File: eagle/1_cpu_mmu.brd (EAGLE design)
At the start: 160 x 100 mm, 49 parts, among them IC1 MT5C6408, IC10 74LS157N, IC11 74LS157N, IC12 74LS00N, IC13 74LS157N, IC14 74LS157N, IC16 74LS08N, IC17 74LS32N, IC19 74LS32N, IC2 MT5C6408, IC20 74LS02N, IC21 74LS374N, IC3 74LS27N, IC4 74LS20N, IC5 74LS08N, IC6 74LS245N, IC7 74LS245N, IC8 74LS32N, IC9 74LS157N

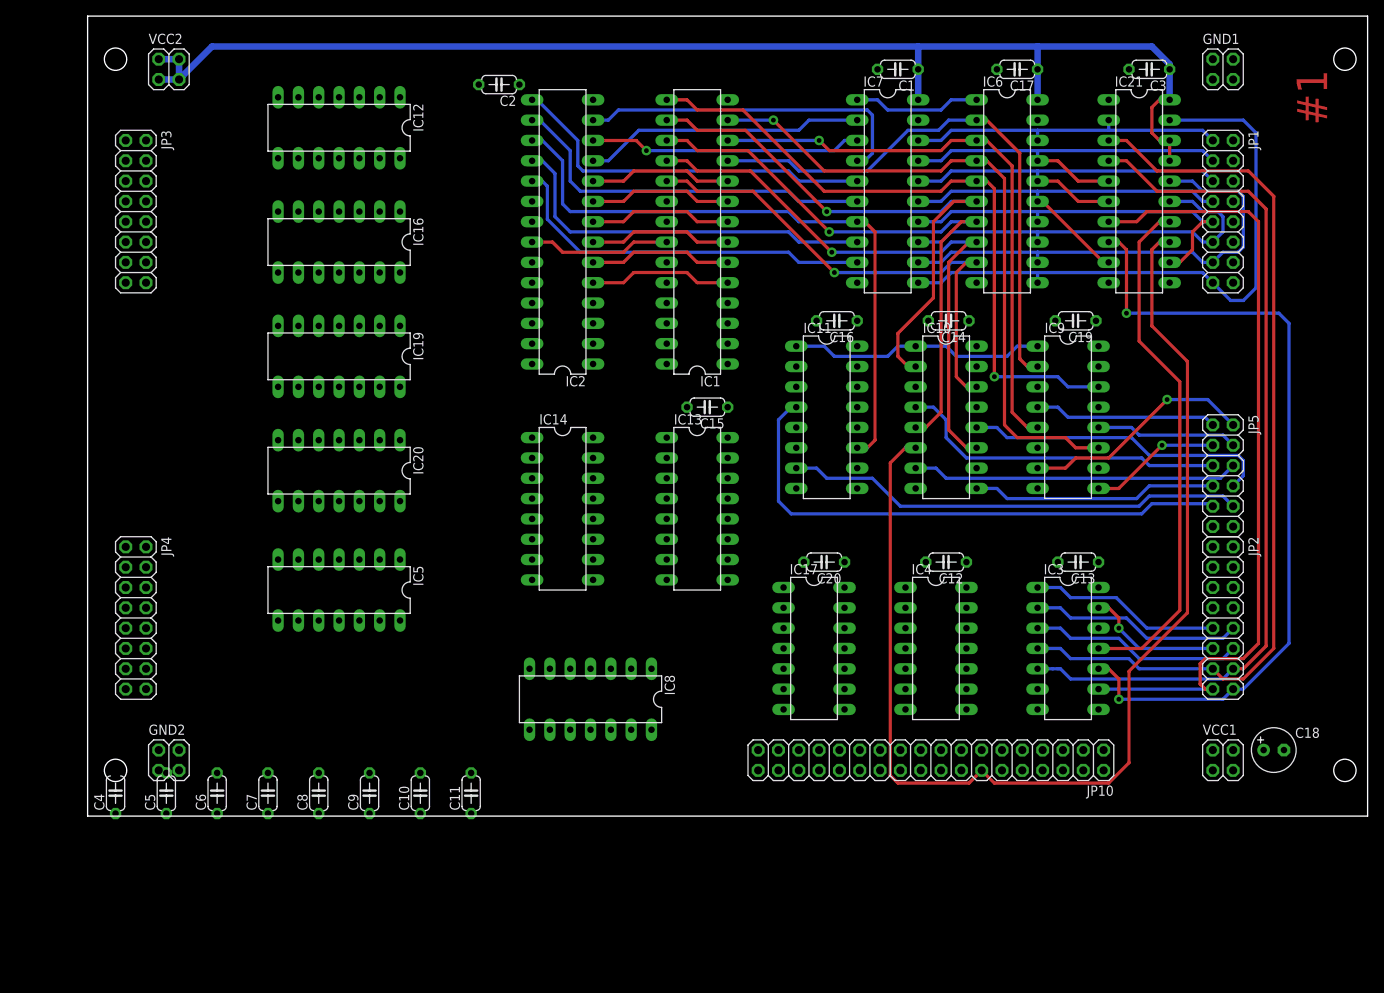
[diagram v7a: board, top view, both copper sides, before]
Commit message: MMU and Memory board updates, removed mem_ext board (obsolete)
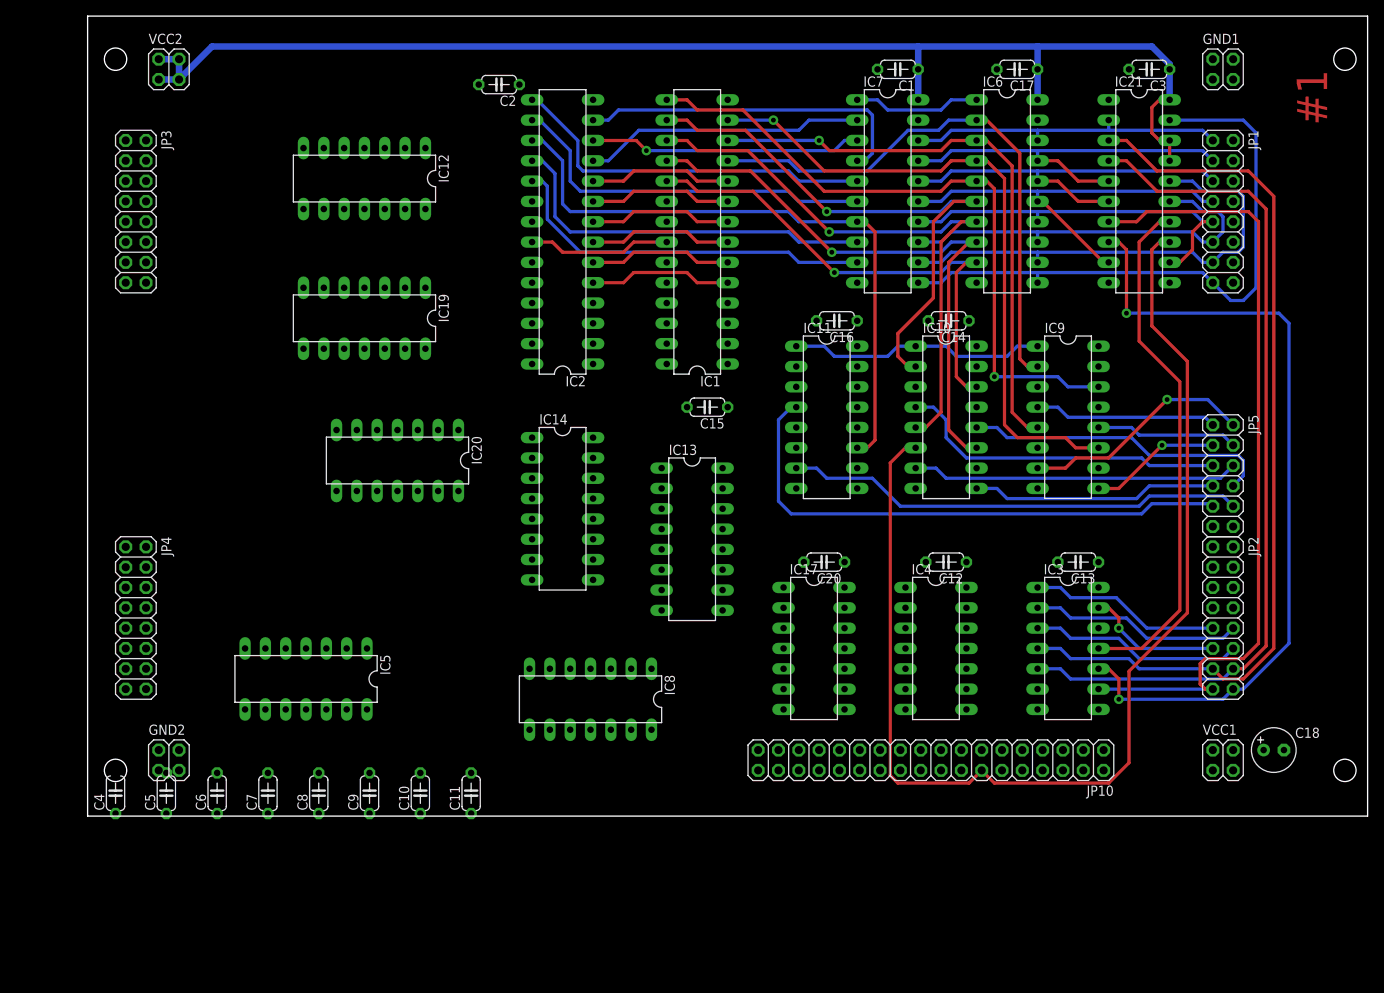
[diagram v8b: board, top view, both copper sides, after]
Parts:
- removed C19: 100n, rcl:C050-024X044
- removed IC16: 74LS08N, 74xx-eu:DIL14
- moved IC5 11.9 mm to (27.3, 17.1)
- moved IC20 7.41 mm to (38.7, 44.5)
- moved IC12 7.10 mm to (34.6, 79.7)
- moved IC19 5.72 mm to (34.6, 62.2)
- moved IC13 3.86 mm to (75.6, 34.6)
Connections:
- net +5V: no longer C19.1, IC16.14
- net /FS: no longer IC20.6
- net /NP_FAULT: no longer IC16.4
- net /WR_FAULT: no longer IC16.5
- net ABUS7: now also IC20.6
- net FAULT: now also IC20.8, IC20.9
- net GND: no longer C19.2, IC16.1, IC16.10, IC16.12, IC16.13, IC16.2, IC16.7, IC16.9, IC20.8, IC20.9
- net N$40: now also IC20.10; no longer IC16.6
